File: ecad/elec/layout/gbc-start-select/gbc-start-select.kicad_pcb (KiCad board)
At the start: 2 copper layers, 5 parts

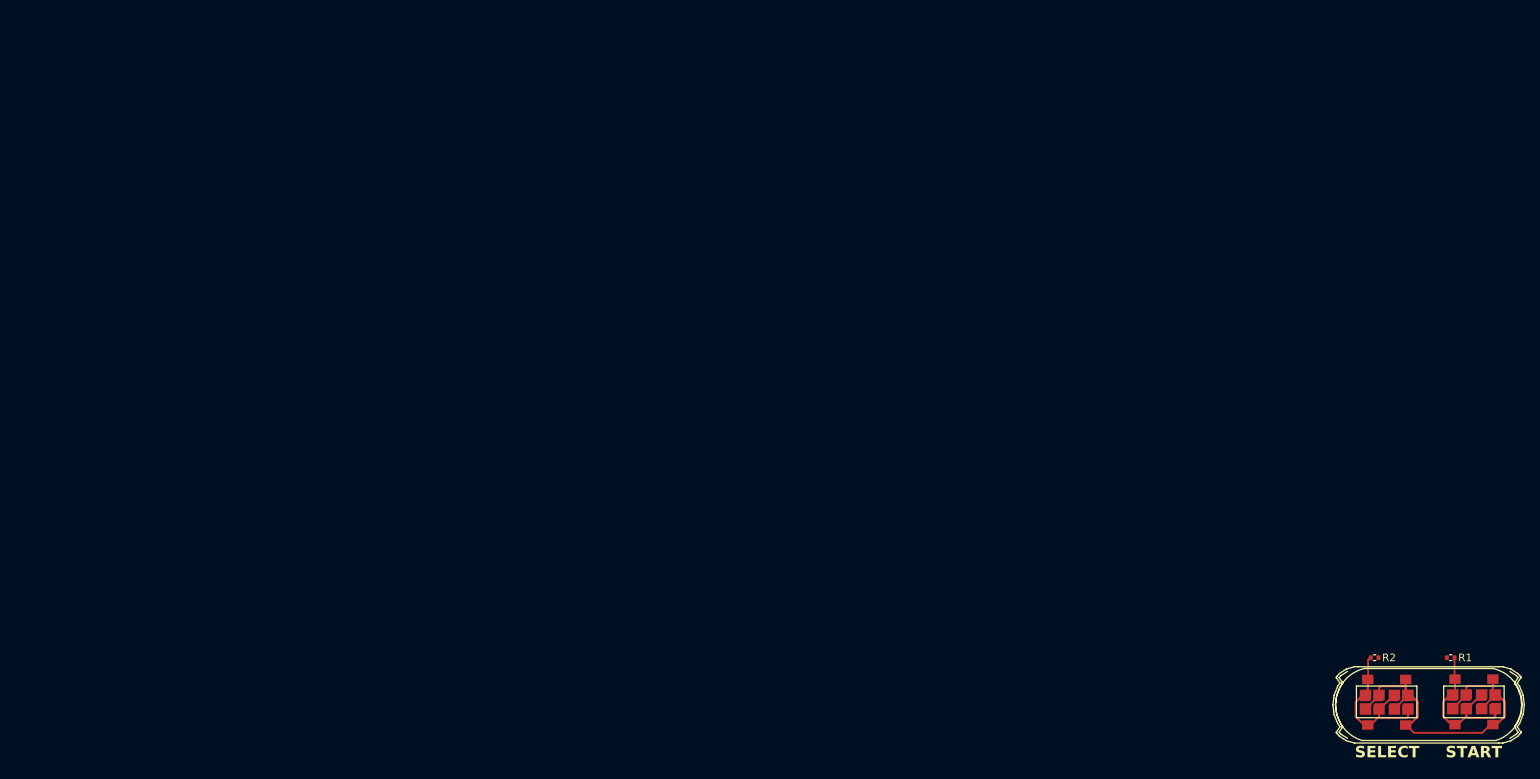
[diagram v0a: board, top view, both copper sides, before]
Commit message: feat(ecad): Update ECAD to support latest atopile and fix some bugs (#119)
* feat(ecad): Update ecad / atopile and improve workflow

* add step file to repo

* add box-3 step file

* improve workflow

* update the action to latest and fix some bugs / spurious issues

* remove legacy files

* update readme

* update deprecations

* improve placement of components and robustness of scripts

* nudge layouts some

* further layout changes

* fixing some issues

* fix broken ci

* minor update

* simple layout

* update to work with latest atopile services (lack thereof)

* update routing

* fix(ecad): vendor atopile registry package for CI builds

packages.atopileapi.com no longer resolves (taken down in the 0.16
platform migration, like the components API), so dependency resolution
of atopile/ti-tps63020@0.4.0 fails in CI and on any machine without a
warm .ato/modules. Commit the installed package (sans .cache) so
`ato build` finds it via its installed-package path and never contacts
the dead registry.

Co-Authored-By: Claude Fable 5 <noreply@anthropic.com>

* fix(ecad): keep vendored package byte-exact (no EOL normalization)

ato validates installed packages against the file hashes in
.package_meta.json; git's CRLF->LF normalization of the STEP files
changed their bytes on checkout, making CI fail with "Package has
local modifications". Exempt ecad/.ato/modules from text normalization
and re-commit the original bytes.

Co-Authored-By: Claude Fable 5 <noreply@anthropic.com>

* fix(ci): disable baked-in ATO_FROZEN and normalize base layout serialization

The atopile-kicad docker image sets ATO_FROZEN=1, silently forcing CI
builds into frozen mode, which fails on phantom in-memory diffs
(locked-attribute defaults, arc direction normalization) that never
reach the file on disk. Pass ATO_FROZEN=0 from the workflow — we verify
layout stability ourselves via canonicalize + git diff.

Also re-serialize box-emu-base.kicad_pcb through the same container
build + canonicalize pip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
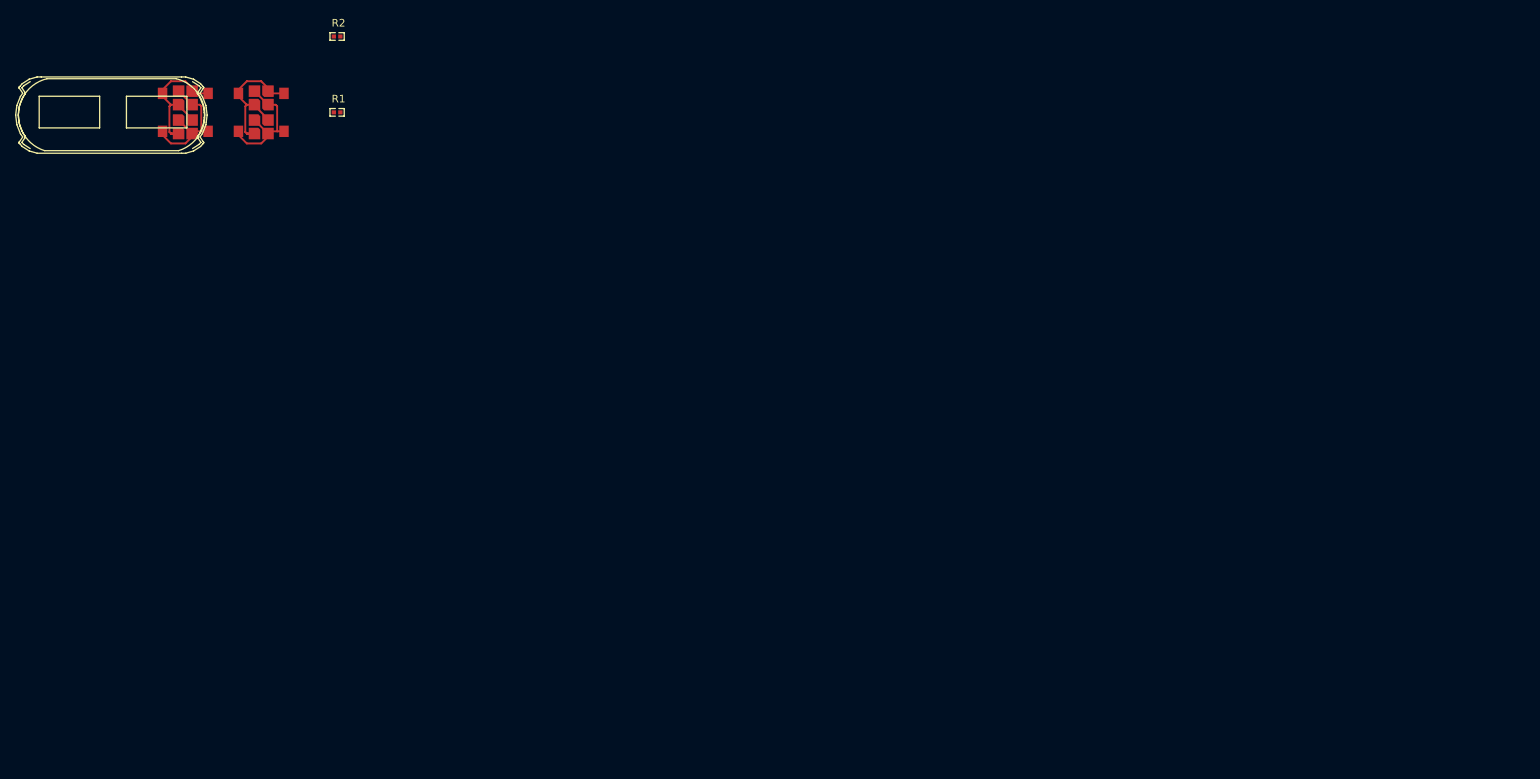
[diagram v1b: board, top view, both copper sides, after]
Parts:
- removed U1: , lib:GAMEBOY_COLOR_START_SELECT_MEMBRANE
- removed U2, U3: , lib:GBC_START_SELECT_BUTTON
- added MECH1: , GBC_START_SELECT_MEMBRANE:GAMEBOY_COLOR_START_SELECT_MEMBRANE, F.Cu at (0.00, 0.00)
- added SW1: , GBC_START_SELECT_BUTTON:GBC_START_SELECT_BUTTON, F.Cu at (20.0, 0.00)
- added SW2: , GBC_START_SELECT_BUTTON:GBC_START_SELECT_BUTTON, F.Cu at (10.0, 0.00)
- R1, R2: value 62.5mW Thick Film Resistors 50V ±100ppm/℃ ±1% 10kΩ 0402 Chip Resistor - Surface Mount ROHS -> 10kΩ ±5%; footprint lib:R0402 -> UNI_ROYAL_0402WGF1002TCE:R0402
- moved R1 163.4 mm to (30.0, 0.00)
- moved R2 159.4 mm to (30.0, -10.0), turned to 0 degrees
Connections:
- net vcc renamed hv
- R1 pad 2: start -> contact_in
- R2 pad 2: select -> start_btn-out-contact_in
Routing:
- net gnd: track 27.6 -> 0.00 mm
- net select: track 10.6 -> 0.00 mm
- net start: track 10.1 -> 0.00 mm
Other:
- board text removed: "SELECT"
- board text removed: "START"
